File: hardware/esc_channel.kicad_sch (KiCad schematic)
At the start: 0 parts

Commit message: wip: schematic sheets in progress
Co-Authored-By: Claude Opus 5.5 <noreply@anthropic.com>
Claude-Session: https://claude.ai/code/session_01RFaS5jnC9tnPam9GBgmGnG
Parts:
- added C19: 100nF, lib:C_0201_0603Metric_W, symbol Device:C
- added C23: 22uF, lib:C_0603_1608Metric_W, symbol Device:C
- added Q29, Q30, Q31: AGM210MAP, lib:AGM_PDFN-8-2EP_3.3x3.3mm_AGM210MAP, symbol lib:AGM210MAP
- added R12: 2.4k, lib:R_0201_0603Metric_W, symbol Device:R
- added R13, R14, R15: 10k, lib:R_0201_0603Metric_W, symbol Device:R
- added R16, R17, R18: 1k, lib:R_0201_0603Metric_W, symbol Device:R
- added TP1: C2D, lib:TestPoint_Via_D0.35mm_Drill0.2mm, symbol Connector:TestPoint
- added TP2: C2CK, lib:TestPoint_Via_D0.35mm_Drill0.2mm, symbol Connector:TestPoint
- added U6: EFM8BB51F16I, lib:QFN-20_3x3mm_P0.5mm_EFM8BB51, symbol lib:EFM8BB51F16I-C-QFN20R
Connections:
- new net +BATT: C19.1, C23.1, Q29.3 (S2), Q30.3 (S2), Q31.3 (S2), U6.4 (VDD)
- new net A_COM: Q29.4 (G2), U6.13 (P1.1)
- new net A_PWM: Q29.2 (G1), U6.14 (P1.0)
- new net BEMF_A: R13.2, U6.19 (P0.3)
- new net BEMF_B: R14.2, U6.1 (P0.1)
- new net BEMF_C: R15.2, U6.20 (P0.2)
- new net B_COM: Q30.4 (G2), U6.10 (P1.3)
- new net B_PWM: Q30.2 (G1), U6.11 (P1.2)
- new net C2CK: TP2.1, U6.5 (RSTb/C2CK)
- new net C2D: TP1.1, U6.6 (P2.0/C2D)
- new net C_COM: Q31.4 (G2), U6.8 (P1.5)
- new net C_PWM: Q31.2 (G1), U6.9 (P1.4)
- new net DSHOT: R12.1
- new net GND: C19.2, C23.2, Q29.1 (S1), Q30.1 (S1), Q31.1 (S1), U6.12 (GND), U6.21 (GND), U6.3 (GND)
- new net NEUTRAL: R16.2, R17.2, R18.2, U6.18 (P0.4)
- new net PHASE_A: Q29.5 (D2), Q29.6 (D2), Q29.7 (D1), Q29.8 (D1), R13.1, R16.1
- new net PHASE_B: Q30.5 (D2), Q30.6 (D2), Q30.7 (D1), Q30.8 (D1), R14.1, R17.1
- new net PHASE_C: Q31.5 (D2), Q31.6 (D2), Q31.7 (D1), Q31.8 (D1), R15.1, R18.1
- new net RTX: R12.2, U6.17 (P0.5)
- no-connect marks 0 -> 4
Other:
- note added: "BEMF network: 10k series + 1k neutral star"
- note added: "C2 test via"
- note added: "C2 test vias"
- note added: "ESC MCU: EFM8BB51, Bluejay BB51 layout A"
- note added: "Half-bridges A/B/C: AGM210MAP P+N, one package per phase"

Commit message: wip: schematic integration in progress (saved after container restart)
Co-Authored-By: Claude Opus 5.5 <noreply@anthropic.com>
Claude-Session: https://claude.ai/code/session_01RFaS5jnC9tnPam9GBgmGnG
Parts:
- C25: renamed from C19; LCSC (none) -> C181047
- renumbered C23 to C29, Q29 to Q32, Q30 to Q33, Q31 to Q34, R12 to R19, R13 to R20, R14 to R21, R15 to R22, R16 to R23, R17 to R24, R18 to R25, TP1 to TP3, TP2 to TP4, U6 to U7
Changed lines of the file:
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@@
 		(in_pos_files no)
 		(dnp no)
-		(property "Reference" "#PWR906"
+		(property "Reference" "#PWR71"
 			(at 55.88 177.8 0)
 			(hide yes)
@@
 			(project "OpenAIO-Whoop"
 				(path "/2c3a7206-1e66-4d43-a02f-491225e20dd6/0021bee0-9959-5c9e-86f0-21e49fa9ce8d"
-					(reference "#PWR914")
+					(reference "#PWR71")
 					(unit 1)
 				)
 				(path "/2c3a7206-1e66-4d43-a02f-491225e20dd6/6d139bfe-ad39-5d26-964c-e430887c2538"
-					(reference "#PWR930")
+					(reference "#PWR87")
 					(unit 1)
 				)
 				(path "/2c3a7206-1e66-4d43-a02f-491225e20dd6/a3c0517e-76c5-5fd7-8d0f-d7e948ad3995"
-					(reference "#PWR922")
+					(reference "#PWR79")
 					(unit 1)
 				)
 				(path "/2c3a7206-1e66-4d43-a02f-491225e20dd6/d67c44eb-67d1-5da8-b7a8-40b16f9433cd"
-					(reference "#PWR906")
+					(reference "#PWR63")
 					(unit 1)
 				)
@@
 		(in_pos_files yes)
 		(dnp no)
-		(property "Reference" "R15"
+		(property "Reference" "R22"
 			(at 156.21 60.96 90)
 			(show_name no)
@@
 		(in_pos_files yes)
 		(dnp no)
-		(property "Reference" "U6"
+		(property "Reference" "U7"
 			(at 78.74 41.91 0)
 			(show_name no)
@@
 		(in_pos_files yes)
 		(dnp no)
-		(property "Reference" "R16"
+		(property "Reference" "R23"
 			(at 156.21 33.02 90)
 			(show_name no)
@@
 		(in_pos_files yes)
 		(dnp no)
-		(property "Reference" "R13"
+		(property "Reference" "R20"
 			(at 156.21 25.4 90)
 			(show_name no)
@@
 		(in_pos_files yes)
 		(dnp no)
-		(property "Reference" "C19"
+		(property "Reference" "C25"
 			(at 60.96 35.56 0)
 			(show_name no)
@@
 			)
 		)
-		(property "LCSC" ""
+		(property "LCSC" "C181047"
 			(at 58.42 36.83 0)
 			(hide yes)
@@
 		(in_pos_files yes)
 		(dnp no)
-		(property "Reference" "R12"
+		(property "Reference" "R19"
 			(at 40.64 63.5 90)
 			(show_name no)
@@
 		(in_pos_files yes)
 		(dnp no)
-		(property "Reference" "Q30"
+		(property "Reference" "Q33"
 			(at 101.6 152.4 0)
 			(show_name no)
@@
 		(in_pos_files no)
 		(dnp no)
-		(property "Reference" "#PWR903"
+		(property "Reference" "#PWR68"
 			(at 76.2 87.63 0)
 			(hide yes)
@@
 			(project "OpenAIO-Whoop"
 				(path "/2c3a7206-1e66-4d43-a02f-491225e20dd6/0021bee0-9959-5c9e-86f0-21e49fa9ce8d"
-					(reference "#PWR911")
+					(reference "#PWR68")
 					(unit 1)
 				)
 				(path "/2c3a7206-1e66-4d43-a02f-491225e20dd6/6d139bfe-ad39-5d26-964c-e430887c2538"
-					(reference "#PWR927")
+					(reference "#PWR84")
 					(unit 1)
 				)
 				(path "/2c3a7206-1e66-4d43-a02f-491225e20dd6/a3c0517e-76c5-5fd7-8d0f-d7e948ad3995"
-					(reference "#PWR919")
+					(reference "#PWR76")
 					(unit 1)
 				)
 				(path "/2c3a7206-1e66-4d43-a02f-491225e20dd6/d67c44eb-67d1-5da8-b7a8-40b16f9433cd"
-					(reference "#PWR903")
+					(reference "#PWR60")
 					(unit 1)
 				)
@@
 		(in_pos_files yes)
 		(dnp no)
-		(property "Reference" "Q31"
+		(property "Reference" "Q34"
 			(at 144.78 152.4 0)
 			(show_name no)
@@
 		(in_pos_files no)
 		(dnp no)
-		(property "Reference" "#PWR907"
+		(property "Reference" "#PWR72"
 			(at 99.06 177.8 0)
 			(hide yes)
@@
 			(project "OpenAIO-Whoop"
 				(path "/2c3a7206-1e66-4d43-a02f-491225e20dd6/0021bee0-9959-5c9e-86f0-21e49fa9ce8d"
-					(reference "#PWR915")
+					(reference "#PWR72")
 					(unit 1)
 				)
 				(path "/2c3a7206-1e66-4d43-a02f-491225e20dd6/6d139bfe-ad39-5d26-964c-e430887c2538"
-					(reference "#PWR931")
+					(reference "#PWR88")
 					(unit 1)
 				)
 				(path "/2c3a7206-1e66-4d43-a02f-491225e20dd6/a3c0517e-76c5-5fd7-8d0f-d7e948ad3995"
-					(reference "#PWR923")
+					(reference "#PWR80")
 					(unit 1)
 				)
 				(path "/2c3a7206-1e66-4d43-a02f-491225e20dd6/d67c44eb-67d1-5da8-b7a8-40b16f9433cd"
-					(reference "#PWR907")
+					(reference "#PWR64")
 					(unit 1)
 				)
@@
 		(in_pos_files yes)
 		(dnp no)
-		(property "Reference" "R18"
+		(property "Reference" "R25"
 			(at 156.21 68.58 90)
 			(show_name no)
@@
 		(in_pos_files no)
 		(dnp no)
-		(property "Reference" "TP1"
+		(property "Reference" "TP3"
 			(at 110.49 64.77 90)
 			(show_name no)
@@
 		(in_pos_files no)
 		(dnp no)
-		(property "Reference" "TP2"
+		(property "Reference" "TP4"
 			(at 41.91 46.99 90)
 			(show_name no)
@@
 		(in_pos_files no)
 		(dnp no)
-		(property "Reference" "#PWR908"
+		(property "Reference" "#PWR73"
 			(at 142.24 177.8 0)
 			(hide yes)
@@
 			(project "OpenAIO-Whoop"
 				(path "/2c3a7206-1e66-4d43-a02f-491225e20dd6/0021bee0-9959-5c9e-86f0-21e49fa9ce8d"
-					(reference "#PWR916")
+					(reference "#PWR73")
 					(unit 1)
 				)
 				(path "/2c3a7206-1e66-4d43-a02f-491225e20dd6/6d139bfe-ad39-5d26-964c-e430887c2538"
-					(reference "#PWR932")
+					(reference "#PWR89")
 					(unit 1)
 				)
 				(path "/2c3a7206-1e66-4d43-a02f-491225e20dd6/a3c0517e-76c5-5fd7-8d0f-d7e948ad3995"
-					(reference "#PWR924")
+					(reference "#PWR81")
 					(unit 1)
 				)
 				(path "/2c3a7206-1e66-4d43-a02f-491225e20dd6/d67c44eb-67d1-5da8-b7a8-40b16f9433cd"
-					(reference "#PWR908")
+					(reference "#PWR65")
 					(unit 1)
 				)
@@
 		(in_pos_files yes)
 		(dnp no)
-		(property "Reference" "R17"
+		(property "Reference" "R24"
 			(at 156.21 50.8 90)
 			(show_name no)
@@
 		(in_pos_files no)
 		(dnp no)
-		(property "Reference" "#PWR905"
+		(property "Reference" "#PWR70"
 			(at 27.94 158.75 0)
 			(hide yes)
@@
 			(project "OpenAIO-Whoop"
 				(path "/2c3a7206-1e66-4d43-a02f-491225e20dd6/0021bee0-9959-5c9e-86f0-21e49fa9ce8d"
-					(reference "#PWR913")
+					(reference "#PWR70")
 					(unit 1)
 				)
 				(path "/2c3a7206-1e66-4d43-a02f-491225e20dd6/6d139bfe-ad39-5d26-964c-e430887c2538"
-					(reference "#PWR929")
+					(reference "#PWR86")
 					(unit 1)
 				)
 				(path "/2c3a7206-1e66-4d43-a02f-491225e20dd6/a3c0517e-76c5-5fd7-8d0f-d7e948ad3995"
-					(reference "#PWR921")
+					(reference "#PWR78")
 					(unit 1)
 				)
 				(path "/2c3a7206-1e66-4d43-a02f-491225e20dd6/d67c44eb-67d1-5da8-b7a8-40b16f9433cd"
-					(reference "#PWR905")
+					(reference "#PWR62")
 					(unit 1)
 				)
@@
 		(in_pos_files no)
 		(dnp no)
-		(property "Reference" "#PWR901"
+		(property "Reference" "#PWR66"
 			(at 76.2 31.75 0)
 			(hide yes)
@@
 			(project "OpenAIO-Whoop"
 				(path "/2c3a7206-1e66-4d43-a02f-491225e20dd6/0021bee0-9959-5c9e-86f0-21e49fa9ce8d"
-					(reference "#PWR909")
+					(reference "#PWR66")
 					(unit 1)
 				)
 				(path "/2c3a7206-1e66-4d43-a02f-491225e20dd6/6d139bfe-ad39-5d26-964c-e430887c2538"
-					(reference "#PWR925")
+					(reference "#PWR82")
 					(unit 1)
 				)
 				(path "/2c3a7206-1e66-4d43-a02f-491225e20dd6/a3c0517e-76c5-5fd7-8d0f-d7e948ad3995"
-					(reference "#PWR917")
+					(reference "#PWR74")
 					(unit 1)
 				)
 				(path "/2c3a7206-1e66-4d43-a02f-491225e20dd6/d67c44eb-67d1-5da8-b7a8-40b16f9433cd"
-					(reference "#PWR901")
+					(reference "#PWR58")
 					(unit 1)
 				)
@@
 		(in_pos_files no)
 		(dnp no)
-		(property "Reference" "#PWR902"
+		(property "Reference" "#PWR67"
 			(at 58.42 49.53 0)
 			(hide yes)
@@
 			(project "OpenAIO-Whoop"
 				(path "/2c3a7206-1e66-4d43-a02f-491225e20dd6/0021bee0-9959-5c9e-86f0-21e49fa9ce8d"
-					(reference "#PWR910")
+					(reference "#PWR67")
 					(unit 1)
 				)
 				(path "/2c3a7206-1e66-4d43-a02f-491225e20dd6/6d139bfe-ad39-5d26-964c-e430887c2538"
-					(reference "#PWR926")
+					(reference "#PWR83")
 					(unit 1)
 				)
 				(path "/2c3a7206-1e66-4d43-a02f-491225e20dd6/a3c0517e-76c5-5fd7-8d0f-d7e948ad3995"
-					(reference "#PWR918")
+					(reference "#PWR75")
 					(unit 1)
 				)
 				(path "/2c3a7206-1e66-4d43-a02f-491225e20dd6/d67c44eb-67d1-5da8-b7a8-40b16f9433cd"
-					(reference "#PWR902")
+					(reference "#PWR59")
 					(unit 1)
 				)
@@
 		(in_pos_files no)
 		(dnp no)
-		(property "Reference" "#PWR904"
+		(property "Reference" "#PWR69"
 			(at 22.86 143.51 0)
 			(hide yes)
@@
 			(project "OpenAIO-Whoop"
 				(path "/2c3a7206-1e66-4d43-a02f-491225e20dd6/0021bee0-9959-5c9e-86f0-21e49fa9ce8d"
-					(reference "#PWR912")
+					(reference "#PWR69")
 					(unit 1)
 				)
 				(path "/2c3a7206-1e66-4d43-a02f-491225e20dd6/6d139bfe-ad39-5d26-964c-e430887c2538"
-					(reference "#PWR928")
+					(reference "#PWR85")
 					(unit 1)
 				)
 				(path "/2c3a7206-1e66-4d43-a02f-491225e20dd6/a3c0517e-76c5-5fd7-8d0f-d7e948ad3995"
-					(reference "#PWR920")
+					(reference "#PWR77")
 					(unit 1)
 				)
 				(path "/2c3a7206-1e66-4d43-a02f-491225e20dd6/d67c44eb-67d1-5da8-b7a8-40b16f9433cd"
-					(reference "#PWR904")
+					(reference "#PWR61")
 					(unit 1)
 				)
@@
 		(in_pos_files yes)
 		(dnp no)
-		(property "Reference" "C23"
+		(property "Reference" "C29"
 			(at 30.48 144.78 0)
 			(show_name no)
@@
 		(in_pos_files yes)
 		(dnp no)
-		(property "Reference" "Q29"
+		(property "Reference" "Q32"
 			(at 58.42 152.4 0)
 			(show_name no)
@@
 		(in_pos_files yes)
 		(dnp no)
-		(property "Reference" "R14"
+		(property "Reference" "R21"
 			(at 156.21 43.18 90)
 			(show_name no)

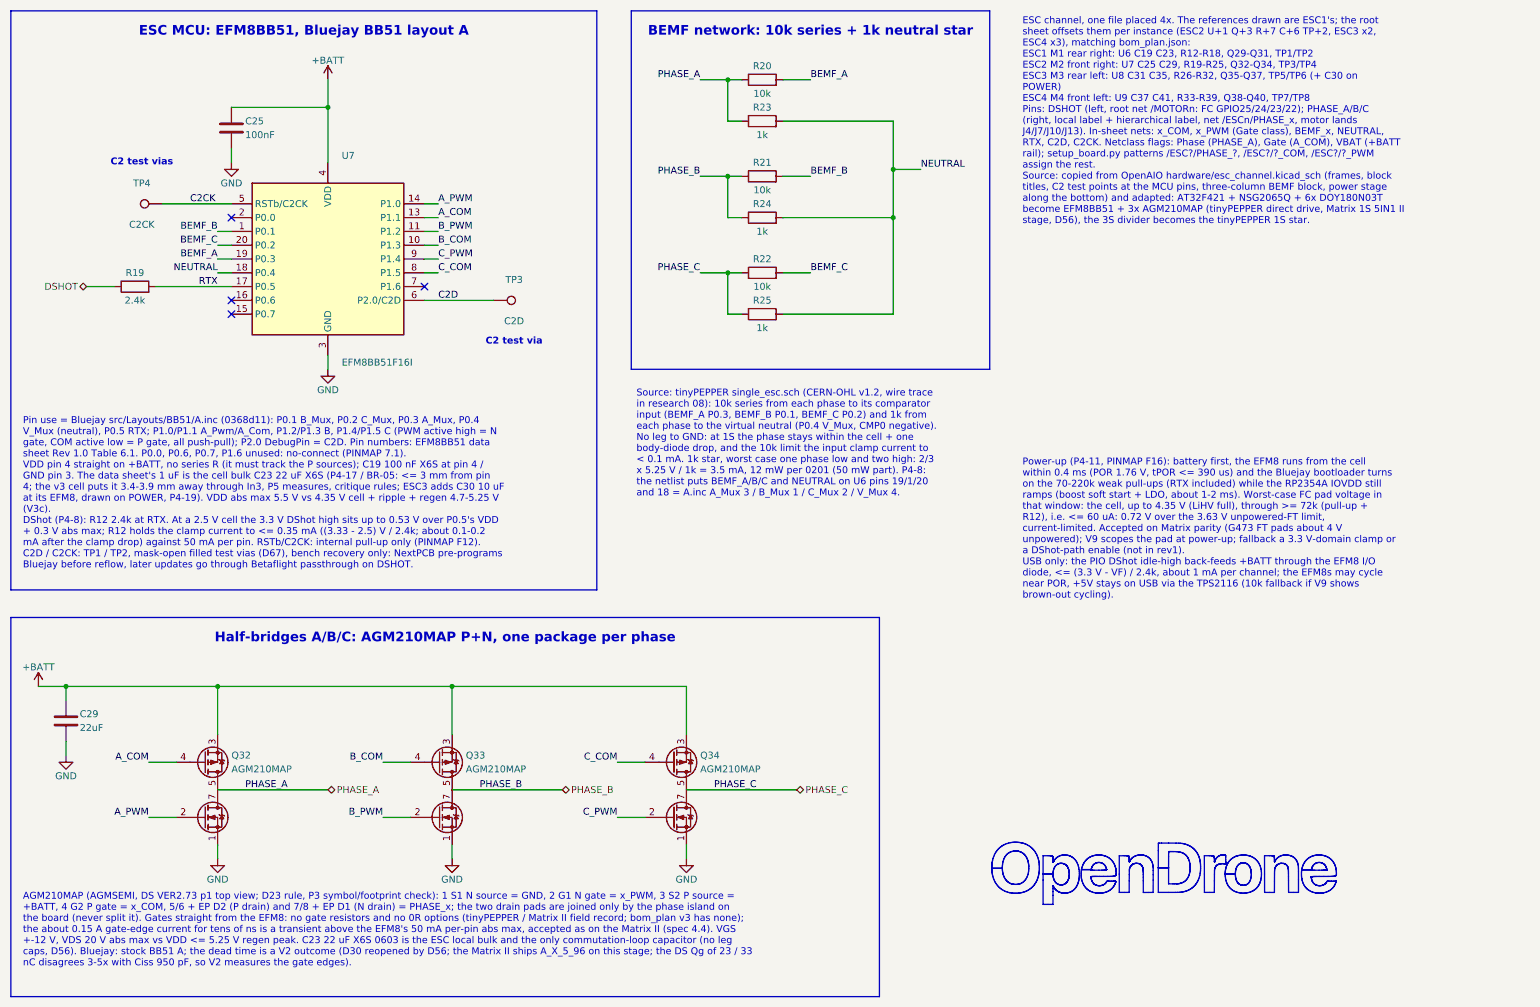
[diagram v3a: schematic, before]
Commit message: schematic: integrated (ERC 0 errors / 2 justified warnings; check_netlist 7/7; conventions 0 FAIL; visual 0 hits; 268/268 refs match bom_plan; FC+RX pin maps match PINMAP)
Co-Authored-By: Claude Opus 5.5 <noreply@anthropic.com>
Claude-Session: https://claude.ai/code/session_01RFaS5jnC9tnPam9GBgmGnG
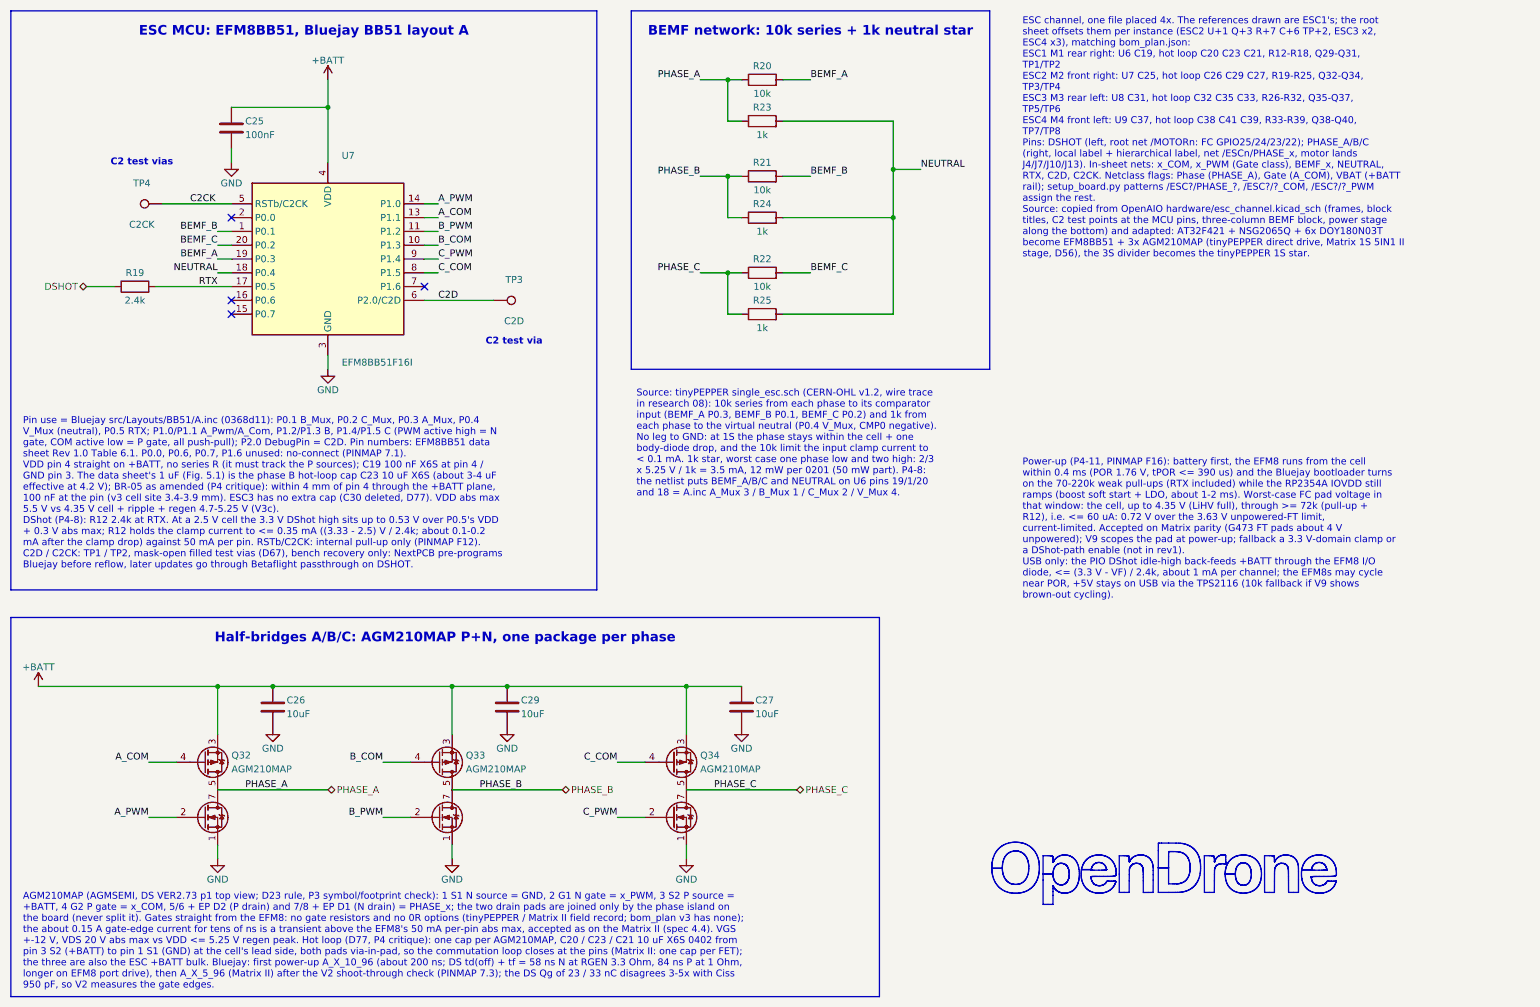
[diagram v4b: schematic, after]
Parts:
- added C26, C27: 10uF, lib:C_0402_1005Metric_W, symbol Device:C
- C29: value 22uF -> 10uF; footprint lib:C_0603_1608Metric_W -> lib:C_0402_1005Metric_W; LCSC C393031 -> C237279; MPN GRM188C80J226ME15D -> GRM155C80J106ME11D
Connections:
- net +BATT: now also C26.1, C27.1
- net GND: now also C26.2, C27.2
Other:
- moved on the sheet: C29
